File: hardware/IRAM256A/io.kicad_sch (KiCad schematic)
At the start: 51 parts

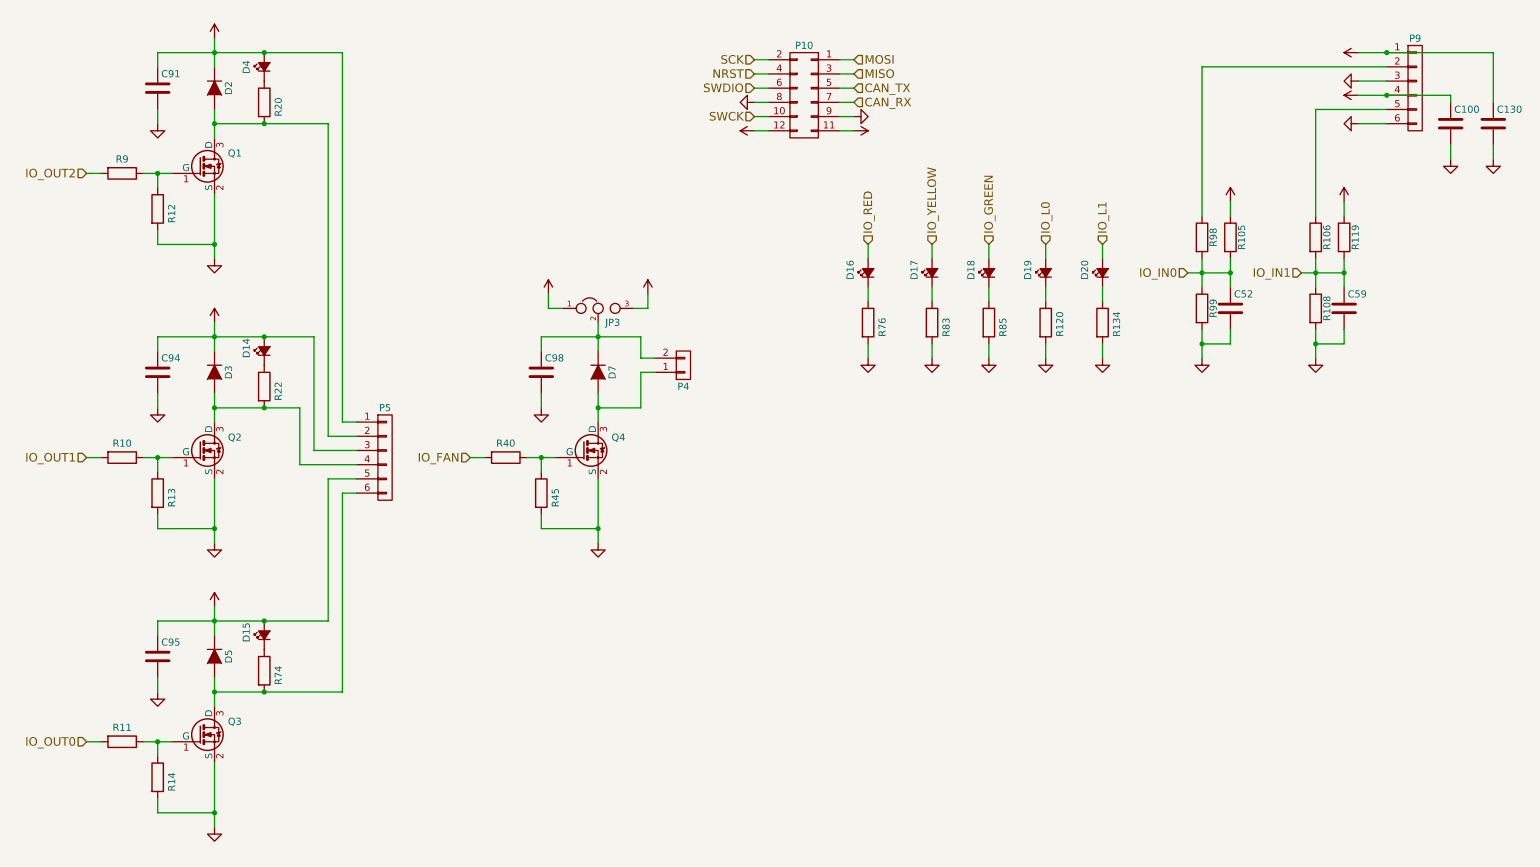
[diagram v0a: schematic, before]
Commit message: Structure change + kicad 3d models updated
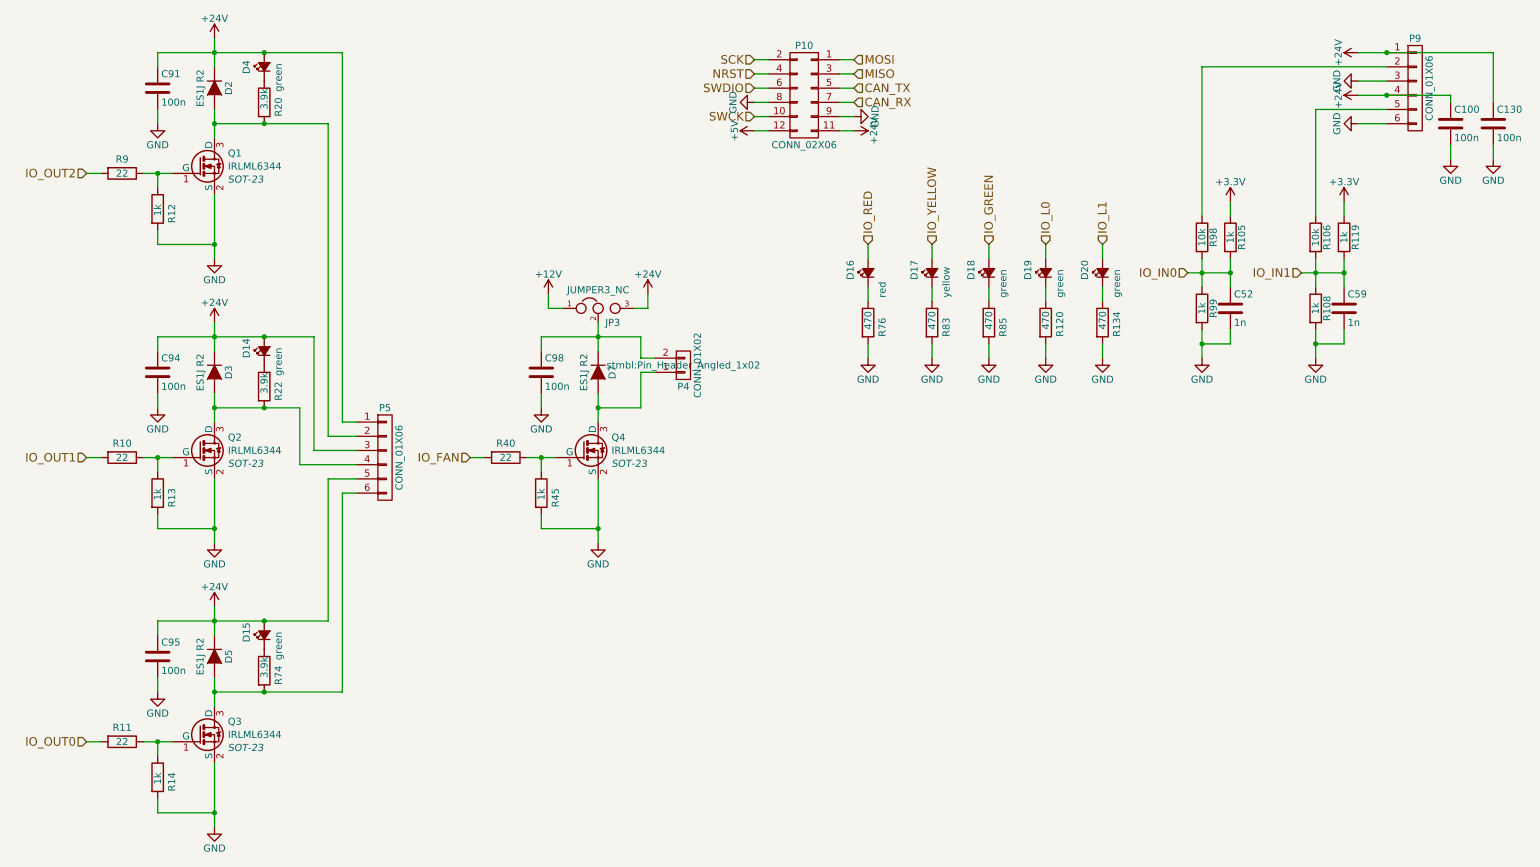
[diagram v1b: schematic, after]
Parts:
- C100, C130, C91, C94, C95, C98: value (none) -> 100n; footprint (none) -> stmbl:C_0603
- C52, C59: value (none) -> 1n; footprint (none) -> stmbl:C_0603
- D14, D15, D18, D19, D20, D4: value (none) -> green; footprint (none) -> stmbl:LED-0805-SIDE
- D16: value (none) -> red; footprint (none) -> stmbl:LED-0805-SIDE
- D17: value (none) -> yellow; footprint (none) -> stmbl:LED-0805-SIDE
- D2, D3, D5, D7: value (none) -> ES1J R2; footprint (none) -> stmbl:SMA_Standard
- JP3: value (none) -> JUMPER3_NC; footprint (none) -> stmbl:SOLDER_JUMPER_3_NC
- P10: value (none) -> CONN_02X06; footprint (none) -> stmbl:Socket_Strip_Angled_2x06
- P4: value (none) -> CONN_01X02; footprint (none) -> stmbl:Pin_Header_Angled_1x02
- P5, P9: value (none) -> CONN_01X06; footprint (none) -> stmbl:RM3.5_1x6
- Q1, Q2, Q3, Q4: value (none) -> IRLML6344; footprint (none) -> SOT-23
- R10, R11, R40, R9: value (none) -> 22; footprint (none) -> stmbl:R_0603
- R105, R108, R119, R12, R13, R14, R45, R99: value (none) -> 1k; footprint (none) -> stmbl:R_0603
- R106, R98: value (none) -> 10k; footprint (none) -> stmbl:R_0603
- R120, R134, R76, R83, R85: value (none) -> 470; footprint (none) -> stmbl:R_0603
- R20, R22, R74: value (none) -> 3.9k; footprint (none) -> stmbl:R_0603
